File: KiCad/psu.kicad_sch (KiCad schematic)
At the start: 20 parts, among them J1 Conn_02x04_Top_Bottom, J2 ATX-24, U6 TPS54331

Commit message: Add most passive component footprints
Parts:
- D21: footprint (none) -> Diode_SMD:D_SMA
- J1: footprint (none) -> Connector_Molex:Molex_Mini-Fit_Jr_5566-08A_2x04_P4.20mm_Vertical
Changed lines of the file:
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@@
 			)
 		)
-		(property "Footprint" ""
+		(property "Footprint" "Diode_SMD:D_SMA"
 			(at 124.46 91.44 90)
 			(effects
@@
 			)
 		)
-		(property "Footprint" ""
+		(property "Footprint" "Connector_Molex:Molex_Mini-Fit_Jr_5566-08A_2x04_P4.20mm_Vertical"
 			(at 48.26 109.22 0)
 			(effects

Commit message: Add m.2 slot footprints
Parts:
- L1: footprint (none) -> Inductor_SMD:L_7.3x7.3_H3.5
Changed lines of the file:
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@@
 			)
 		)
-		(property "Footprint" ""
+		(property "Footprint" "Inductor_SMD:L_7.3x7.3_H3.5"
 			(at 134.62 83.82 0)
 			(effects

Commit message: Finish fixing footprints
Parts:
- renumbered C136 to C130, C130 to C131, C131 to C132, C132 to C133, C137 to C134, C138 to C135, C133 to C136, C134 to C137, C135 to C138, J2 to J1, J1 to J2, R103 to R101, R101 to R103
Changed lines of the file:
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@@
 		(dnp no)
 		(fields_autoplaced yes)
-		(property "Reference" "#PWR097"
+		(property "Reference" "#PWR0111"
 			(at 58.42 109.22 0)
 			(effects
@@
 			(project ""
 				(path "/49abeb3a-c598-45a3-ba6b-595eb04f17a8/73807de7-58af-4eca-b212-2dba82ac67f9"
-					(reference "#PWR097")
+					(reference "#PWR0111")
 					(unit 1)
 				)
@@
 		(on_board yes)
 		(dnp no)
-		(property "Reference" "C138"
+		(property "Reference" "C135"
 			(at 148.844 85.852 0)
 			(effects
@@
 			(project "LattePandaMuCluster"
 				(path "/49abeb3a-c598-45a3-ba6b-595eb04f17a8/73807de7-58af-4eca-b212-2dba82ac67f9"
-					(reference "C138")
+					(reference "C135")
 					(unit 1)
 				)
@@
 		(dnp no)
 		(fields_autoplaced yes)
-		(property "Reference" "#PWR0108"
+		(property "Reference" "#PWR0104"
 			(at 179.07 83.82 0)
 			(effects
@@
 			(project ""
 				(path "/49abeb3a-c598-45a3-ba6b-595eb04f17a8/73807de7-58af-4eca-b212-2dba82ac67f9"
-					(reference "#PWR0108")
+					(reference "#PWR0104")
 					(unit 1)
 				)
@@
 		(dnp no)
 		(fields_autoplaced yes)
-		(property "Reference" "C136"
+		(property "Reference" "C130"
 			(at 127.0063 73.66 90)
 			(effects
@@
 			(project ""
 				(path "/49abeb3a-c598-45a3-ba6b-595eb04f17a8/73807de7-58af-4eca-b212-2dba82ac67f9"
-					(reference "C136")
+					(reference "C130")
 					(unit 1)
 				)
@@
 		(dnp no)
 		(fields_autoplaced yes)
-		(property "Reference" "#FLG08"
+		(property "Reference" "#FLG06"
 			(at 187.96 61.595 0)
 			(effects
@@
 			(project ""
 				(path "/49abeb3a-c598-45a3-ba6b-595eb04f17a8/73807de7-58af-4eca-b212-2dba82ac67f9"
-					(reference "#FLG08")
+					(reference "#FLG06")
 					(unit 1)
 				)
@@
 		(dnp no)
 		(fields_autoplaced yes)
-		(property "Reference" "#PWR0103"
+		(property "Reference" "#PWR0110"
 			(at 97.79 110.49 0)
 			(effects
@@
 			(project ""
 				(path "/49abeb3a-c598-45a3-ba6b-595eb04f17a8/73807de7-58af-4eca-b212-2dba82ac67f9"
-					(reference "#PWR0103")
+					(reference "#PWR0110")
 					(unit 1)
 				)
@@
 		(on_board yes)
 		(dnp no)
-		(property "Reference" "C133"
+		(property "Reference" "C136"
 			(at 96.266 91.948 90)
 			(effects
@@
 			(project ""
 				(path "/49abeb3a-c598-45a3-ba6b-595eb04f17a8/73807de7-58af-4eca-b212-2dba82ac67f9"
-					(reference "C133")
+					(reference "C136")
 					(unit 1)
 				)
@@
 		(dnp no)
 		(fields_autoplaced yes)
-		(property "Reference" "#PWR099"
+		(property "Reference" "#PWR0100"
 			(at 73.66 63.5 0)
 			(effects
@@
 			(project ""
 				(path "/49abeb3a-c598-45a3-ba6b-595eb04f17a8/73807de7-58af-4eca-b212-2dba82ac67f9"
-					(reference "#PWR099")
+					(reference "#PWR0100")
 					(unit 1)
 				)
@@
 		(dnp no)
 		(fields_autoplaced yes)
-		(property "Reference" "#FLG06"
+		(property "Reference" "#FLG08"
 			(at 58.42 117.475 0)
 			(effects
@@
 			(project ""
 				(path "/49abeb3a-c598-45a3-ba6b-595eb04f17a8/73807de7-58af-4eca-b212-2dba82ac67f9"
-					(reference "#FLG06")
+					(reference "#FLG08")
 					(unit 1)
 				)
@@
 		(on_board yes)
 		(dnp no)
-		(property "Reference" "C135"
+		(property "Reference" "C138"
 			(at 101.346 91.948 90)
 			(effects
@@
 			(project "LattePandaMuCluster"
 				(path "/49abeb3a-c598-45a3-ba6b-595eb04f17a8/73807de7-58af-4eca-b212-2dba82ac67f9"
-					(reference "C135")
+					(reference "C138")
 					(unit 1)
 				)
@@
 		(on_board yes)
 		(dnp no)
-		(property "Reference" "C130"
+		(property "Reference" "C131"
 			(at 79.502 84.582 90)
 			(effects
@@
 			(project "LattePandaMuCluster"
 				(path "/49abeb3a-c598-45a3-ba6b-595eb04f17a8/73807de7-58af-4eca-b212-2dba82ac67f9"
-					(reference "C130")
+					(reference "C131")
 					(unit 1)
 				)
@@
 		(dnp no)
 		(fields_autoplaced yes)
-		(property "Reference" "#PWR0107"
+		(property "Reference" "#PWR0103"
 			(at 179.07 67.31 0)
 			(effects
@@
 			(project ""
 				(path "/49abeb3a-c598-45a3-ba6b-595eb04f17a8/73807de7-58af-4eca-b212-2dba82ac67f9"
-					(reference "#PWR0107")
+					(reference "#PWR0103")
 					(unit 1)
 				)
@@
 		(on_board yes)
 		(dnp no)
-		(property "Reference" "C137"
+		(property "Reference" "C134"
 			(at 142.494 85.852 0)
 			(effects
@@
 			(project ""
 				(path "/49abeb3a-c598-45a3-ba6b-595eb04f17a8/73807de7-58af-4eca-b212-2dba82ac67f9"
-					(reference "C137")
+					(reference "C134")
 					(unit 1)
 				)
@@
 		(dnp no)
 		(fields_autoplaced yes)
-		(property "Reference" "#PWR0102"
+		(property "Reference" "#PWR0107"
 			(at 83.82 97.79 0)
 			(effects
@@
 			(project ""
 				(path "/49abeb3a-c598-45a3-ba6b-595eb04f17a8/73807de7-58af-4eca-b212-2dba82ac67f9"
-					(reference "#PWR0102")
+					(reference "#PWR0107")
 					(unit 1)
 				)
@@
 		(dnp no)
 		(fields_autoplaced yes)
-		(property "Reference" "#PWR0101"
+		(property "Reference" "#PWR0102"
 			(at 85.09 63.5 0)
 			(effects
@@
 			(project ""
 				(path "/49abeb3a-c598-45a3-ba6b-595eb04f17a8/73807de7-58af-4eca-b212-2dba82ac67f9"
-					(reference "#PWR0101")
+					(reference "#PWR0102")
 					(unit 1)
 				)
@@
 		(on_board yes)
 		(dnp no)
-		(property "Reference" "J1"
+		(property "Reference" "J2"
 			(at 49.53 100.33 0)
 			(effects
@@
 			(project ""
 				(path "/49abeb3a-c598-45a3-ba6b-595eb04f17a8/73807de7-58af-4eca-b212-2dba82ac67f9"
-					(reference "J1")
+					(reference "J2")
 					(unit 1)
 				)
@@
 		(on_board yes)
 		(dnp no)
-		(property "Reference" "R103"
+		(property "Reference" "R101"
 			(at 134.62 85.852 90)
 			(effects
@@
 			(project ""
 				(path "/49abeb3a-c598-45a3-ba6b-595eb04f17a8/73807de7-58af-4eca-b212-2dba82ac67f9"
-					(reference "R103")
+					(reference "R101")
 					(unit 1)
 				)
@@
 		(on_board yes)
 		(dnp no)
-		(property "Reference" "#PWR0104"
+		(property "Reference" "#PWR0108"
 			(at 111.76 100.33 0)
 			(effects
@@
 			(project ""
 				(path "/49abeb3a-c598-45a3-ba6b-595eb04f17a8/73807de7-58af-4eca-b212-2dba82ac67f9"
-					(reference "#PWR0104")
+					(reference "#PWR0108")
 					(unit 1)
 				)
@@
 		(dnp no)
 		(fields_autoplaced yes)
-		(property "Reference" "#PWR096"
+		(property "Reference" "#PWR0106"
 			(at 52.07 90.17 0)
 			(effects
@@
 			(project ""
 				(path "/49abeb3a-c598-45a3-ba6b-595eb04f17a8/73807de7-58af-4eca-b212-2dba82ac67f9"
-					(reference "#PWR096")
+					(reference "#PWR0106")
 					(unit 1)
 				)
@@
 		(on_board yes)
 		(dnp no)
-		(property "Reference" "#PWR0105"
+		(property "Reference" "#PWR0109"
 			(at 124.46 102.87 0)
 			(effects
@@
 			(project ""
 				(path "/49abeb3a-c598-45a3-ba6b-595eb04f17a8/73807de7-58af-4eca-b212-2dba82ac67f9"
-					(reference "#PWR0105")
+					(reference "#PWR0109")
 					(unit 1)
 				)
@@
 		(on_board yes)
 		(dnp no)
-		(property "Reference" "C132"
+		(property "Reference" "C133"
 			(at 84.582 84.582 90)
 			(effects
@@
 			(project ""
 				(path "/49abeb3a-c598-45a3-ba6b-595eb04f17a8/73807de7-58af-4eca-b212-2dba82ac67f9"
-					(reference "C132")
+					(reference "C133")
 					(unit 1)
 				)
@@
 		(on_board yes)
 		(dnp no)
-		(property "Reference" "R101"
+		(property "Reference" "R103"
 			(at 100.584 100.076 0)
 			(effects
@@
 			(project ""
 				(path "/49abeb3a-c598-45a3-ba6b-595eb04f17a8/73807de7-58af-4eca-b212-2dba82ac67f9"
-					(reference "R101")
+					(reference "R103")
 					(unit 1)
 				)
@@
 		(dnp no)
 		(fields_autoplaced yes)
-		(property "Reference" "#PWR0100"
+		(property "Reference" "#PWR0101"
 			(at 78.74 63.5 0)
 			(effects
@@
 			(project ""
 				(path "/49abeb3a-c598-45a3-ba6b-595eb04f17a8/73807de7-58af-4eca-b212-2dba82ac67f9"
-					(reference "#PWR0100")
+					(reference "#PWR0101")
 					(unit 1)
 				)
@@
 		(dnp no)
 		(fields_autoplaced yes)
-		(property "Reference" "#PWR098"
+		(property "Reference" "#PWR099"
 			(at 68.58 63.5 0)
 			(effects
@@
 			(project ""
 				(path "/49abeb3a-c598-45a3-ba6b-595eb04f17a8/73807de7-58af-4eca-b212-2dba82ac67f9"
-					(reference "#PWR098")
+					(reference "#PWR099")
 					(unit 1)
 				)
@@
 		(on_board yes)
 		(dnp no)
-		(property "Reference" "C131"
+		(property "Reference" "C132"
 			(at 82.042 84.582 90)
 			(effects
@@
 			(project "LattePandaMuCluster"
 				(path "/49abeb3a-c598-45a3-ba6b-595eb04f17a8/73807de7-58af-4eca-b212-2dba82ac67f9"
-					(reference "C131")
+					(reference "C132")
 					(unit 1)
 				)
@@
 		(dnp no)
 		(fields_autoplaced yes)
-		(property "Reference" "J2"
+		(property "Reference" "J1"
 			(at 52.07 48.26 0)
 			(effects
@@
 			(project ""
 				(path "/49abeb3a-c598-45a3-ba6b-595eb04f17a8/73807de7-58af-4eca-b212-2dba82ac67f9"
-					(reference "J2")
+					(reference "J1")
 					(unit 1)
 				)
@@
 		(on_board yes)
 		(dnp no)
-		(property "Reference" "#PWR0106"
+		(property "Reference" "#PWR0105"
 			(at 148.59 86.36 0)
 			(effects
@@
 			(project "LattePandaMuCluster"
 				(path "/49abeb3a-c598-45a3-ba6b-595eb04f17a8/73807de7-58af-4eca-b212-2dba82ac67f9"
-					(reference "#PWR0106")
+					(reference "#PWR0105")
 					(unit 1)
 				)
@@
 		(dnp no)
 		(fields_autoplaced yes)
-		(property "Reference" "#PWR095"
+		(property "Reference" "#PWR0112"
 			(at 40.64 121.92 0)
 			(effects
@@
 			(project ""
 				(path "/49abeb3a-c598-45a3-ba6b-595eb04f17a8/73807de7-58af-4eca-b212-2dba82ac67f9"
-					(reference "#PWR095")
+					(reference "#PWR0112")
 					(unit 1)
 				)
@@
 		(on_board yes)
 		(dnp no)
-		(property "Reference" "C134"
+		(property "Reference" "C137"
 			(at 98.806 91.948 90)
 			(effects
@@
 			(project ""
 				(path "/49abeb3a-c598-45a3-ba6b-595eb04f17a8/73807de7-58af-4eca-b212-2dba82ac67f9"
-					(reference "C134")
-					(unit 1)
-				)
+					(reference "C137")
+					(unit 1)
+				)

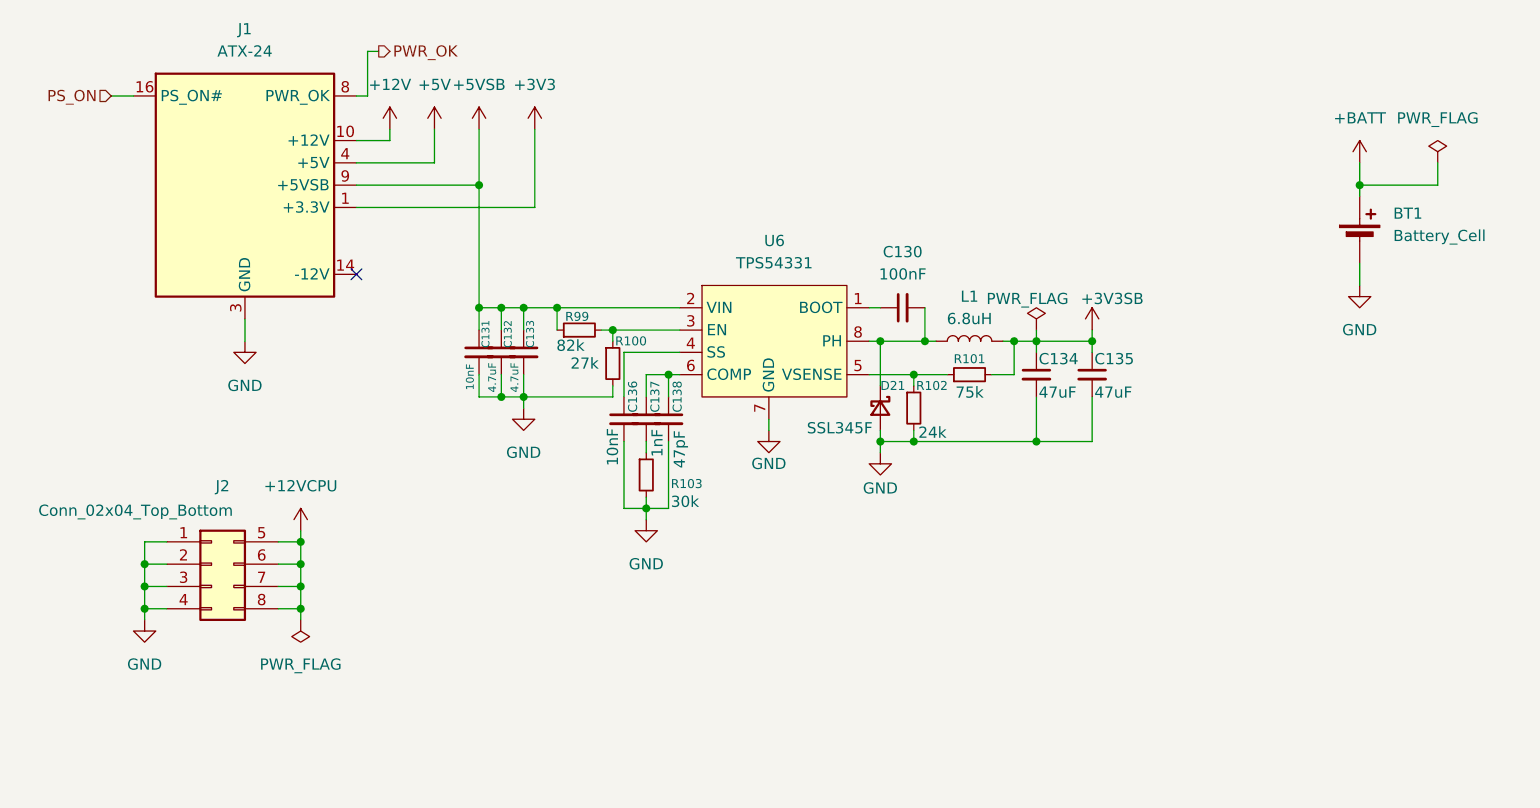
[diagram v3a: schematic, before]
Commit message: Add 0.95V supply, Fix connectors
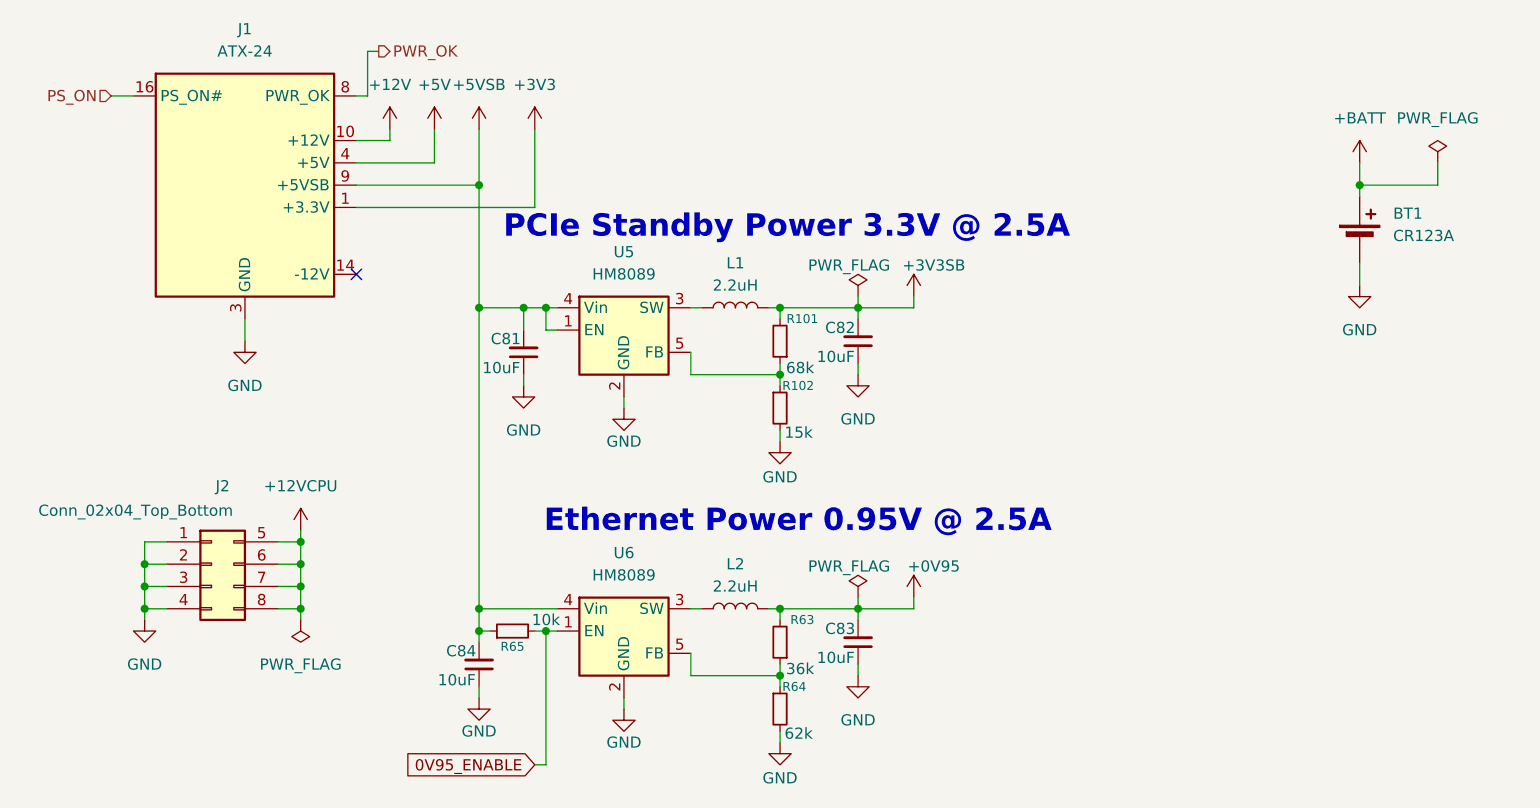
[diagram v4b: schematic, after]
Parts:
- removed C130: 100nF, Capacitor_SMD:C_0402_1005Metric, symbol Device:C_Small
- removed C131, C136: 10nF, Capacitor_SMD:C_0402_1005Metric, symbol Device:C_Small
- removed C132, C133: 4.7uF, Capacitor_SMD:C_0402_1005Metric, symbol Device:C_Small
- removed C134, C135: 47uF, Capacitor_SMD:C_0805_2012Metric, symbol Device:C_Small
- removed C137: 1nF, Capacitor_SMD:C_0402_1005Metric, symbol Device:C_Small
- removed C138: 47pF, Capacitor_SMD:C_0402_1005Metric, symbol Device:C_Small
- removed D21: SSL345F, Diode_SMD:D_SMA, symbol Device:D_Schottky_Small
- removed R100: 27k, Resistor_SMD:R_0603_1608Metric, symbol Device:R_Small
- removed R103: 30k, Resistor_SMD:R_0603_1608Metric, symbol Device:R_Small
- removed R99: 82k, Resistor_SMD:R_0603_1608Metric, symbol Device:R_Small
- removed U6: TPS54331, Package_SO:SOIC-8_3.9x4.9mm_P1.27mm, symbol Custom:TPS54331
- added C81, C82, C83, C84: 10uF, Capacitor_SMD:C_0402_1005Metric, symbol Device:C_Small
- added L2: 2.2uH, Inductor_SMD:L_7.3x7.3_H3.5, symbol Device:L
- added R63: 36k, Resistor_SMD:R_0603_1608Metric, symbol Device:R_Small
- added R64: 62k, Resistor_SMD:R_0603_1608Metric, symbol Device:R_Small
- added R65: 10k, Resistor_SMD:R_0402_1005Metric, symbol Device:R_Small
- added U5, U6: HM8089, Package_TO_SOT_SMD:TSOT-23-5, symbol Regulator_Switching:ADP2108AUJ-1.0
- BT1: value Battery_Cell -> CR123A
- L1: value 6.8uH -> 2.2uH
- R101: value 75k -> 68k
- R102: value 24k -> 15k
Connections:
- net +3V3SB: now also C82.2
- net +5VSB: now also C81.2, C84.2, R65.1, U5.1 (EN), U5.4 (Vin), U6.4 (Vin)
- net GND: now also C81.1, C82.1, C83.1, C84.1, R64.2, U5.2 (GND), U6.2 (GND)
- net at L1.1: now also U5.3 (SW)
- net at R101.1, R102.1: now also U5.5 (FB)
- new net: R63.1, R64.1, U6.5 (FB)
- new net: L2.1, U6.3 (SW)
- new net +0V95: C83.2, L2.2, R63.2
- new net 0V95_ENABLE: R65.2, U6.1 (EN)
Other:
- note added: "Ethernet Power 0.95V @ 2.5A"
- note added: "PCIe Standby Power 3.3V @ 2.5A"
- moved on the sheet: L1, R101, R102
